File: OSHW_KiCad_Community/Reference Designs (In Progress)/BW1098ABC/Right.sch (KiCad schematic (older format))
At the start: 13 parts, among them J6 BBR43-24KB533 for camera modu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

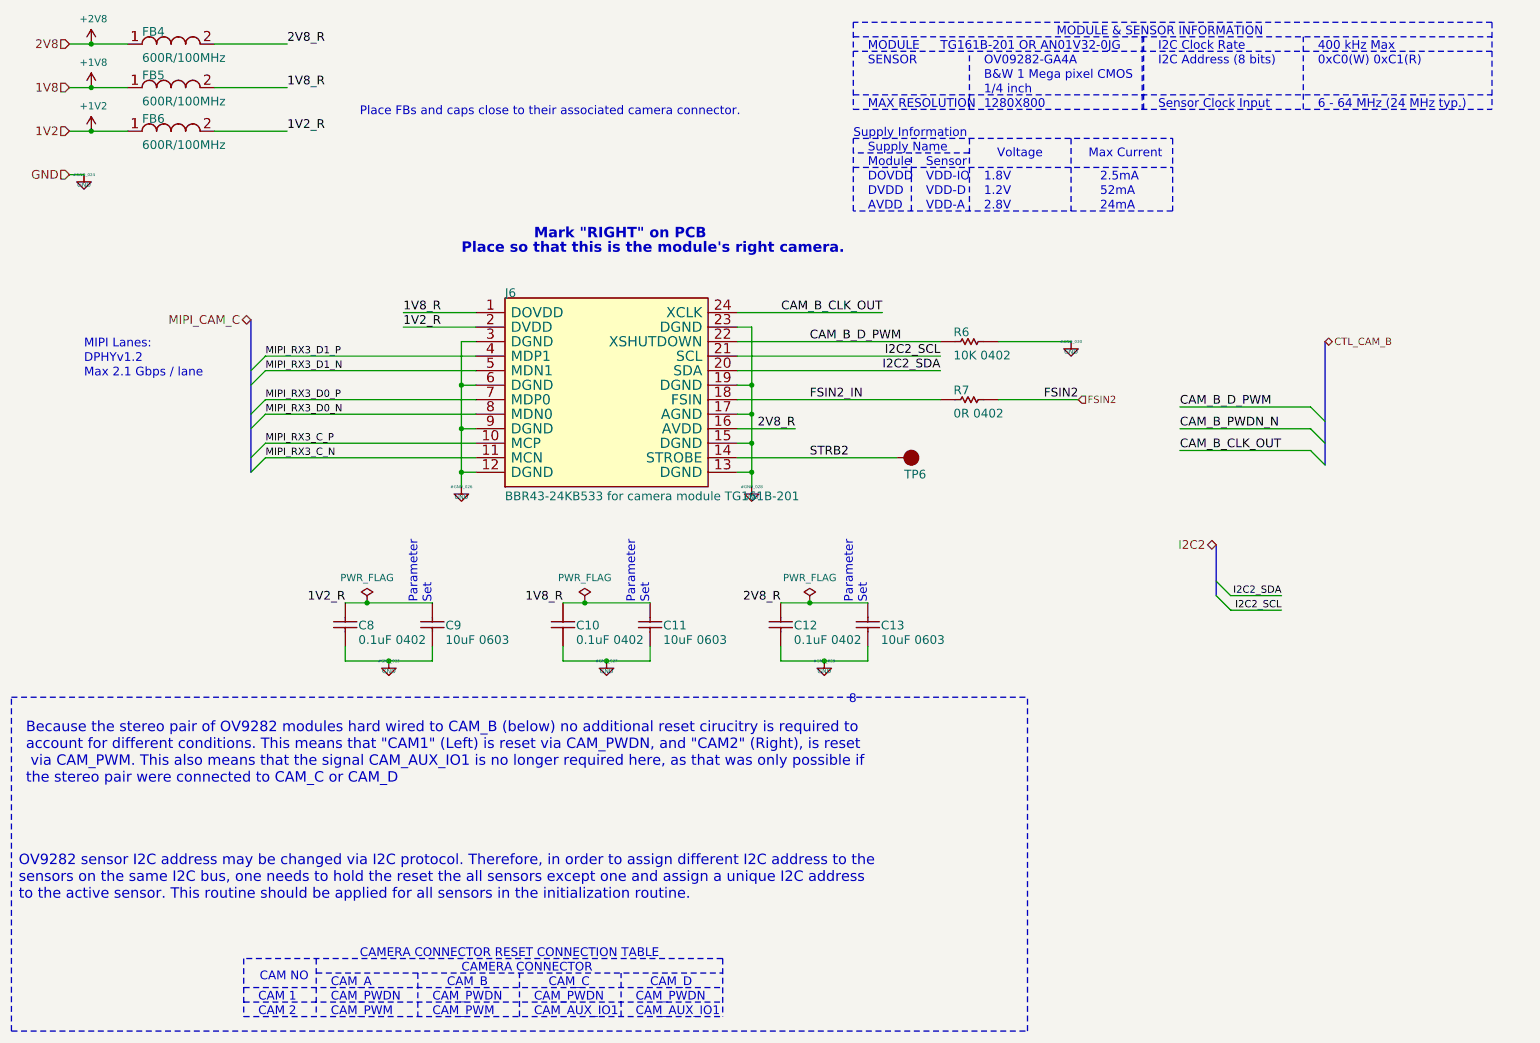
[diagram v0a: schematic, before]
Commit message: BW1098ABC - added back in usbc, got rid of hierarchical labeling in favor of globals. Passes ERC
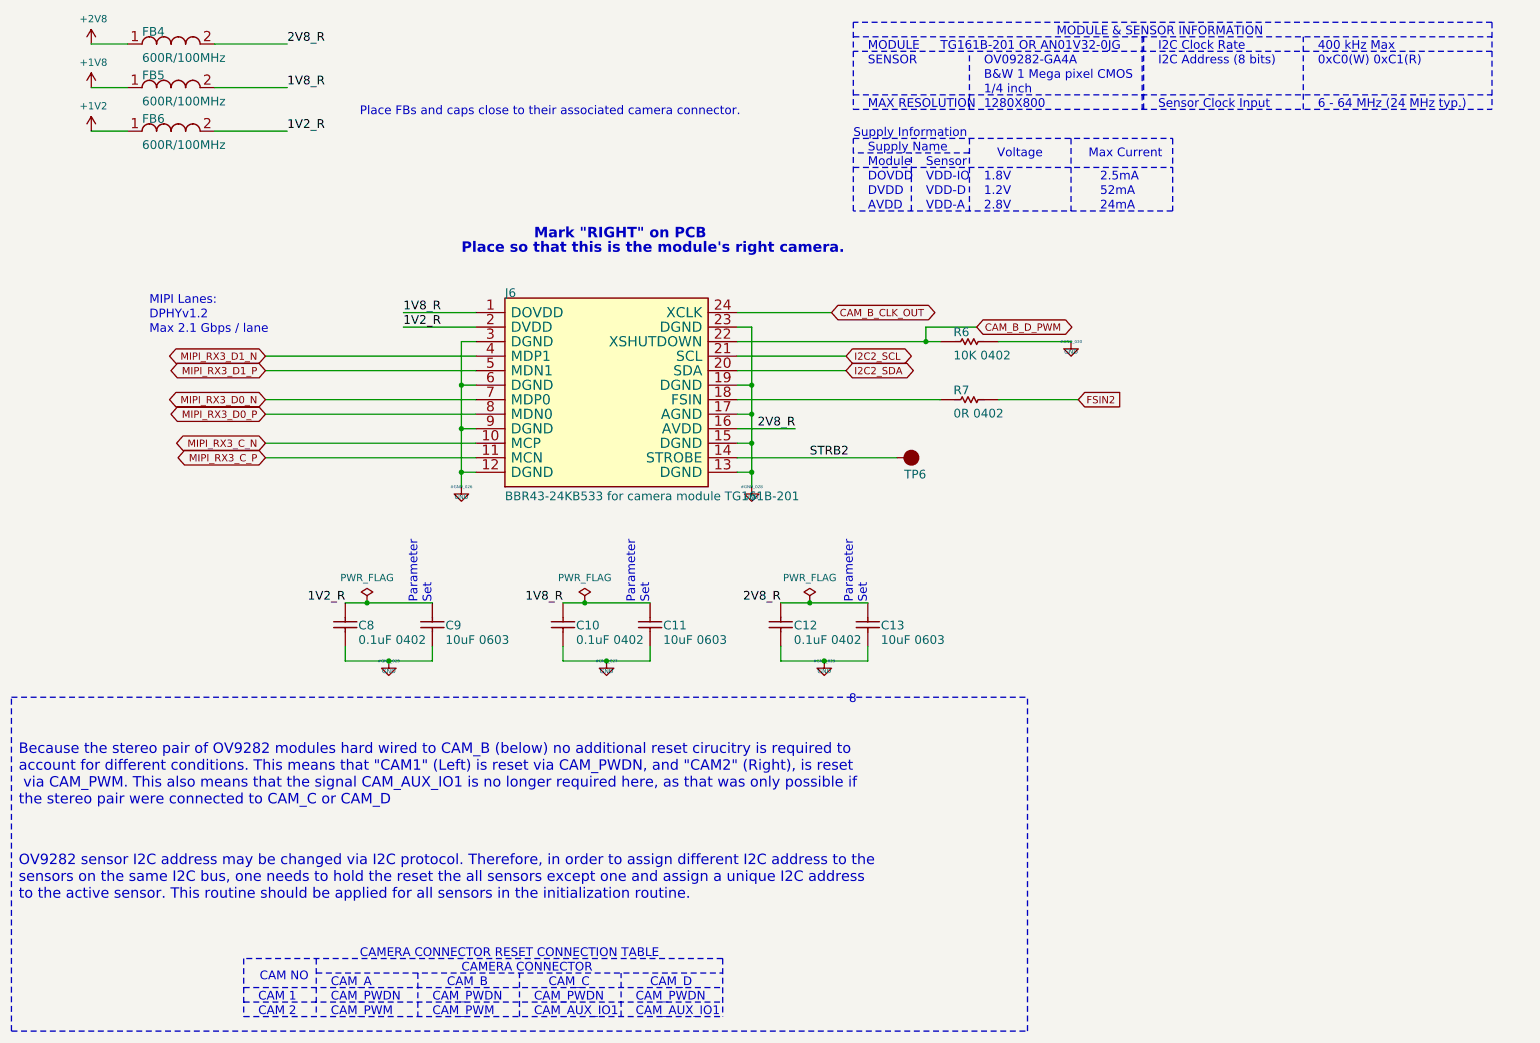
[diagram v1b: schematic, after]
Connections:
- net MIPI_RX3_C_N: now also J6.10 (MCP); no longer J6.11 (MCN)
- net MIPI_RX3_C_P: now also J6.11 (MCN); no longer J6.10 (MCP)
- net MIPI_RX3_D0_N: now also J6.7 (MDP0); no longer J6.8 (MDN0)
- net MIPI_RX3_D0_P: now also J6.8 (MDN0); no longer J6.7 (MDP0)
- net MIPI_RX3_D1_N: now also J6.4 (MDP1); no longer J6.5 (MDN1)
- net MIPI_RX3_D1_P: now also J6.5 (MDN1); no longer J6.4 (MDP1)
- net FSIN2_IN: no longer names the net of J6.18 (FSIN), R7.1
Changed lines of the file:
@@
 $Descr A4 11693 8268
 encoding utf-8
-Sheet 3 6
+Sheet 3 7
 Title ""
 Date ""
@@
 Wire Notes Line
 	6350 1550 8550 1550
-Wire Wire Line
-	950  1000 1100 1000
-Wire Wire Line
-	950  700  1100 700
-Wire Wire Line
-	950  1300 1100 1300
 Text Notes 2950 1200 0    60   ~ 0
 Place FBs and caps close to their associated camera connector.
-Wire Wire Line
-	5550 2950 6950 2950
 Text Notes 600  6600 0    72   ~ 0
 OV9282 sensor I2C address may be changed via I2C protocol. Therefore, in order to assign different I2C address to the \nsensors on the same I2C bus, one needs to hold the reset the all sensors except one and assign a unique I2C address \nto the active sensor. This routine should be applied for all sensors in the initialization routine.
-Text Notes 650  5800 0    72   ~ 0
+Text Notes 600  5950 0    72   ~ 0
 Because the stereo pair of OV9282 modules hard wired to CAM_B (below) no additional reset cirucitry is required to \naccount for different conditions. This means that "CAM1" (Left) is reset via CAM_PWDN, and "CAM2" (Right), is reset\n via CAM_PWM. This also means that the signal CAM_AUX_IO1 is no longer required here, as that was only possible if \nthe stereo pair were connected to CAM_C or CAM_D
 Text Notes 6450 4550 1    60   ~ 0
@@
 	7350 2750 7850 2750
 Wire Wire Line
-	5550 2750 6950 2750
+	5550 2750 6850 2750
 Wire Wire Line
 	5650 3750 5650 3650
@@
 Wire Wire Line
 	6950 3150 5550 3150
-Wire Wire Line
-	5550 2550 6550 2550
 Wire Wire Line
 	3450 4850 3450 4950
@@
 Text Label 6050 3550 0    60   ~ 0
 STRB2
-Text Label 6050 3150 0    60   ~ 0
-FSIN2_IN
 Text Notes 2950 7000 0    60   ~ 0
 CAMERA CONNECTOR RESET CONNECTION TABLE
@@
 Wire Notes Line
 	550  7500 550  5200
-Text HLabel 2200 2600 0    60   BiDi ~ 0
-MIPI_CAM_C
-Text Notes 1050 2900 0    60   ~ 0
+Text Notes 1500 2600 0    60   ~ 0
 DPHYv1.2
-Text Notes 1050 3000 0    60   ~ 0
+Text Notes 1500 2700 0    60   ~ 0
 Max 2.1 Gbps / lane
-Text Notes 1050 2800 0    60   ~ 0
+Text Notes 1500 2500 0    60   ~ 0
 MIPI Lanes:
 $Comp
@@
 	1    0    0    -1
 $EndComp
-Text Label 6050 2750 0    60   ~ 0
-CAM_B_D_PWM
-Text Label 6550 2550 2    60   ~ 0
-CAM_B_CLK_OUT
-Text Label 6950 2850 2    60   ~ 0
-I2C2_SCL
-Text Label 6950 2950 2    60   ~ 0
-I2C2_SDA
 Text Notes 3650 2150 0    72   ~ 14
 Place so that this is the module's right camera.
-Text Label 7900 3150 2    60   ~ 0
-FSIN2
 $Comp
 L power:GND #GND_?
@@
 	1    0    0    -1
 $EndComp
-Connection ~ 1100 700
 Wire Wire Line
 	1100 700  1350 700
-Connection ~ 1100 1000
 Wire Wire Line
 	1100 1000 1350 1000
-Connection ~ 1100 1300
 Wire Wire Line
 	1100 1300 1350 1300
-Text HLabel 950  700  0    60   Input ~ 0
-2V8
-Text HLabel 950  1000 0    60   Input ~ 0
-1V8
-Text HLabel 950  1300 0    60   Input ~ 0
-1V2
-Wire Wire Line
-	5550 2850 6950 2850
-Text HLabel 7900 3150 2    50   Input ~ 0
-FSIN2
 Text Notes 4950 4550 1    60   ~ 0
 Parameter \nSet\n
@@
 Wire Wire Line
 	3000 4550 2850 4550
-Text HLabel 8850 4150 0    60   BiDi ~ 0
-I2C2
-Text Label 9300 4500 2    50   ~ 0
-I2C2_SDA
-Text Label 9300 4600 2    50   ~ 0
-I2C2_SCL
-Entry Wire Line
-	8850 4500 8950 4600
-Entry Wire Line
-	8850 4400 8950 4500
-Wire Wire Line
-	8950 4500 9300 4500
-Wire Wire Line
-	9300 4600 8950 4600
-Text Label 8600 3350 0    60   ~ 0
-CAM_B_PWDN_N
-Wire Wire Line
-	9500 3350 8600 3350
-Wire Wire Line
-	9500 3500 8600 3500
-Entry Wire Line
-	9500 3350 9600 3450
-Entry Wire Line
-	9500 3500 9600 3600
-Text HLabel 9600 2750 2    50   BiDi ~ 0
-CTL_CAM_B
-Text Label 8600 3500 0    60   ~ 0
-CAM_B_CLK_OUT
-Wire Wire Line
-	8600 3200 9500 3200
-Entry Wire Line
-	9500 3200 9600 3300
-Text Label 8600 3200 0    60   ~ 0
-CAM_B_D_PWM
 Wire Wire Line
 	3750 2850 2300 2850
@@
 Wire Wire Line
 	2300 3550 3750 3550
-Text Label 2300 2950 0    50   ~ 0
-MIPI_RX3_D1_N
-Text Label 2300 2850 0    50   ~ 0
-MIPI_RX3_D1_P
-Text Label 2300 3250 0    50   ~ 0
-MIPI_RX3_D0_N
-Text Label 2300 3150 0    50   ~ 0
-MIPI_RX3_D0_P
-Text Label 2300 3550 0    50   ~ 0
-MIPI_RX3_C_N
-Text Label 2300 3450 0    50   ~ 0
-MIPI_RX3_C_P
-Entry Wire Line
-	2300 2850 2200 2950
-Entry Wire Line
-	2300 2950 2200 3050
-Entry Wire Line
-	2300 3150 2200 3250
-Entry Wire Line
-	2300 3250 2200 3350
-Entry Wire Line
-	2300 3450 2200 3550
-Entry Wire Line
-	2300 3550 2200 3650
 Text Label 2450 700  0    60   ~ 0
 2V8_R
@@
 Text Label 2450 1300 0    60   ~ 0
 1V2_R
-Wire Wire Line
-	1050 1600 950  1600
-$Comp
-L power:GND #GND_?
-U 1 1 6041DD77
-P 1050 1600
-AR Path="/5FD7EFD1/6041DD77" Ref="#GND_?"  Part="1"
-AR Path="/5FF8D40A/6041DD77" Ref="#GND_024"  Part="1"
-F 0 "#GND_024" H 1050 1600 20  0000 C CNN
-F 1 "GND" H 1050 1530 30  0000 C CNN
-F 2 "" H 1050 1600 70  0000 C CNN
-F 3 "" H 1050 1600 70  0000 C CNN
-	1    1050 1600
-	1    0    0    -1
-$EndComp
-Text HLabel 950  1600 0    60   Input ~ 0
-GND
 Text Label 5950 3350 2    60   ~ 0
 2V8_R
@@
 Wire Wire Line
 	7350 3150 7900 3150
-Wire Bus Line
-	8850 4150 8850 4500
-Wire Bus Line
-	9600 2750 9600 3600
-Wire Bus Line
-	2200 2600 2200 3650
+Text GLabel 7200 2650 2    50   BiDi ~ 0
+CAM_B_D_PWM
+Text GLabel 6200 2550 2    50   BiDi ~ 0
+CAM_B_CLK_OUT
+Text GLabel 2300 2850 0    50   BiDi ~ 0
+MIPI_RX3_D1_N
+Text GLabel 2300 2950 0    50   BiDi ~ 0
+MIPI_RX3_D1_P
+Text GLabel 2300 3150 0    50   BiDi ~ 0
+MIPI_RX3_D0_N
+Text GLabel 2300 3250 0    50   BiDi ~ 0
+MIPI_RX3_D0_P
+Text GLabel 2300 3450 0    50   BiDi ~ 0
+MIPI_RX3_C_N
+Text GLabel 2300 3550 0    50   BiDi ~ 0
+MIPI_RX3_C_P
+Wire Wire Line
+	7200 2650 6850 2650
+Wire Wire Line
+	6850 2650 6850 2750
+Connection ~ 6850 2750
+Wire Wire Line
+	6850 2750 6950 2750
+Wire Wire Line
+	6200 2550 5550 2550
+Text GLabel 7900 3150 2    50   Input ~ 0
+FSIN2
+Text GLabel 6300 2950 2    50   BiDi ~ 0
+I2C2_SDA
+Text GLabel 6300 2850 2    50   BiDi ~ 0
+I2C2_SCL
+Wire Wire Line
+	6300 2850 5550 2850
+Wire Wire Line
+	5550 2950 6300 2950
 $EndSCHEMATC

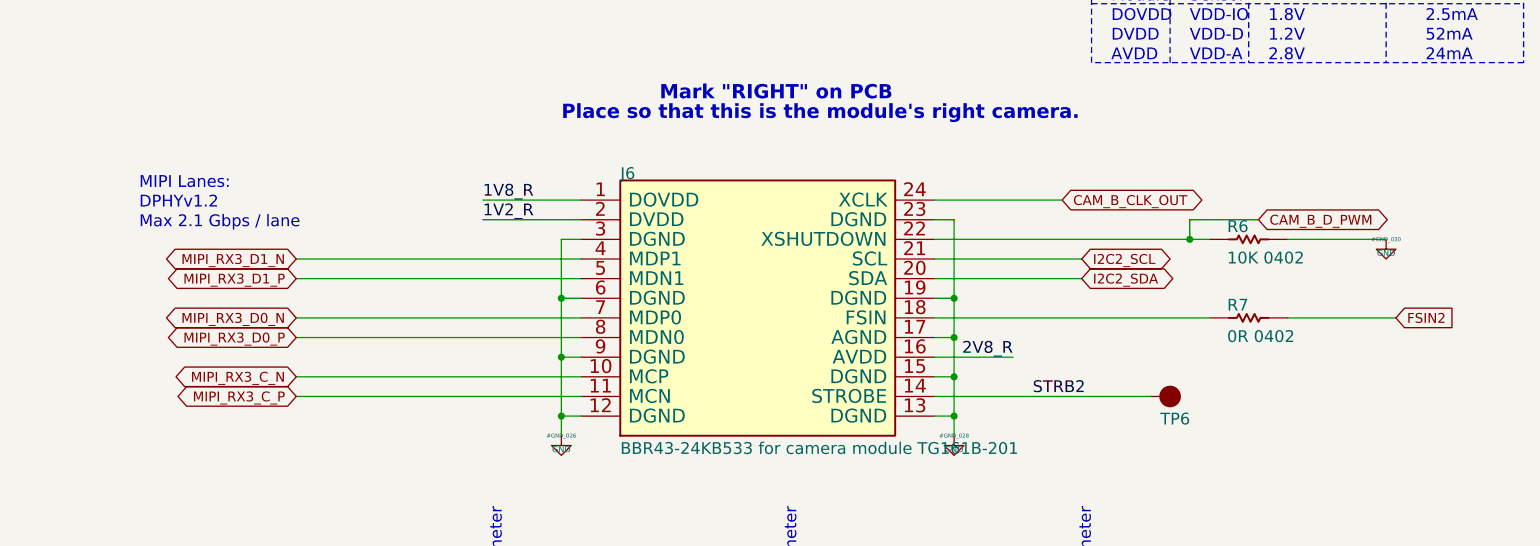
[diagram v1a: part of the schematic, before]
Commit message: going through footprints and datasheet stuff
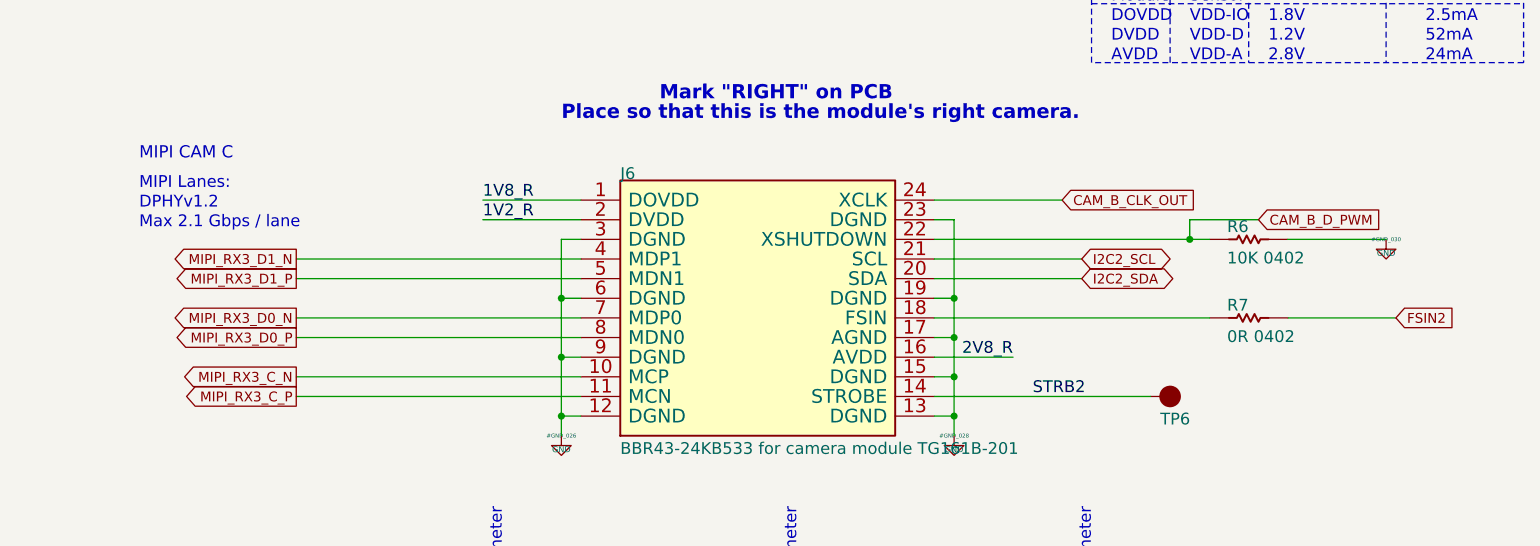
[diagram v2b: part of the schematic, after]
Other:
- note added: "MIPI CAM C"
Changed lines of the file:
@@
 Wire Wire Line
 	7350 3150 7900 3150
-Text GLabel 7200 2650 2    50   BiDi ~ 0
+Text GLabel 7200 2650 2    50   Input ~ 0
 CAM_B_D_PWM
-Text GLabel 6200 2550 2    50   BiDi ~ 0
+Text GLabel 6200 2550 2    50   Input ~ 0
 CAM_B_CLK_OUT
-Text GLabel 2300 2850 0    50   BiDi ~ 0
+Text GLabel 2300 2850 0    50   Output ~ 0
 MIPI_RX3_D1_N
-Text GLabel 2300 2950 0    50   BiDi ~ 0
+Text GLabel 2300 2950 0    50   Output ~ 0
 MIPI_RX3_D1_P
-Text GLabel 2300 3150 0    50   BiDi ~ 0
+Text GLabel 2300 3150 0    50   Output ~ 0
 MIPI_RX3_D0_N
-Text GLabel 2300 3250 0    50   BiDi ~ 0
+Text GLabel 2300 3250 0    50   Output ~ 0
 MIPI_RX3_D0_P
-Text GLabel 2300 3450 0    50   BiDi ~ 0
+Text GLabel 2300 3450 0    50   Output ~ 0
 MIPI_RX3_C_N
-Text GLabel 2300 3550 0    50   BiDi ~ 0
+Text GLabel 2300 3550 0    50   Output ~ 0
 MIPI_RX3_C_P
 Wire Wire Line
@@
 Wire Wire Line
 	5550 2950 6300 2950
+Text Notes 1500 2350 0    62   ~ 0
+MIPI CAM C
 $EndSCHEMATC

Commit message: both camera connector footprints completed
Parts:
- FB4, FB5, FB6: footprint OSHW_LuxonisMaster_20201223:2508056017Y2 -> Luxonis_Kicad_Master:2508056017Y2
- J6: footprint (none) -> Luxonis_Kicad_Master:ACON_BBR43-24KB533
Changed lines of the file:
@@
 F 0 "FB4" H 1450 750 60  0000 L BNN
 F 1 "600R/100MHz" H 1450 570 60  0000 L BNN
-F 2 "OSHW_LuxonisMaster_20201223:2508056017Y2" H 1450 570 60  0001 C CNN
+F 2 "Luxonis_Kicad_Master:2508056017Y2" H 1450 570 60  0001 C CNN
 F 3 "" H 1450 570 60  0000 C CNN
 	1    1350 700
@@
 F 0 "FB5" H 1450 1050 60  0000 L BNN
 F 1 "600R/100MHz" H 1450 870 60  0000 L BNN
-F 2 "OSHW_LuxonisMaster_20201223:2508056017Y2" H 1450 870 60  0001 C CNN
+F 2 "Luxonis_Kicad_Master:2508056017Y2" H 1450 870 60  0001 C CNN
 F 3 "" H 1450 870 60  0000 C CNN
 	1    1350 1000
@@
 F 0 "FB6" H 1450 1350 60  0000 L BNN
 F 1 "600R/100MHz" H 1450 1170 60  0000 L BNN
-F 2 "OSHW_LuxonisMaster_20201223:2508056017Y2" H 1450 1170 60  0001 C CNN
+F 2 "Luxonis_Kicad_Master:2508056017Y2" H 1450 1170 60  0001 C CNN
 F 3 "" H 1450 1170 60  0000 C CNN
 	1    1350 1300
@@
 F 0 "J6" H 3950 2650 60  0000 L BNN
 F 1 "BBR43-24KB533 for camera module TG161B-201" H 3950 1250 60  0000 L BNN
-F 2 "" H 3950 1250 60  0001 C CNN
+F 2 "Luxonis_Kicad_Master:ACON_BBR43-24KB533" H 3950 1250 60  0001 C CNN
 F 3 "" H 3950 1250 60  0000 C CNN
 	1    3750 2550
